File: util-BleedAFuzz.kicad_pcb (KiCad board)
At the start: 2 copper layers, 9.5 x 21.2 mm, 5 parts, among them J1 Conn_01x03_Pin, Q1 BC847, Q2 BC847

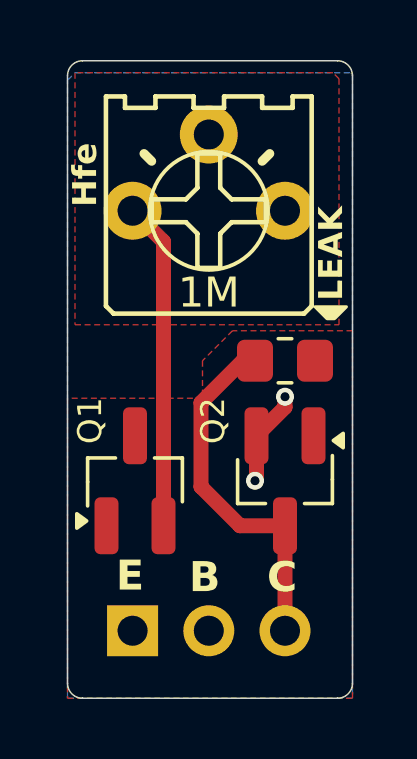
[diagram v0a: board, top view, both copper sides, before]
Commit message: Bleed-a-Fuzz: single transistor with 1M fixed + 1M trimmer base-emitter bleed
Q1 sits straight across the E-B-C header; R2 1M in series with RV1 1M
(rheostat) from base to emitter bleeds base drive so the host stage biases
as if the transistor had a lower hFE (1M..2M covers ~70..140 in a 50 uA
collector-feedback stage such as the Overcast's Q1, ~190..240 in a
fuzz-face Q1 slot). R1 2.2M collector-base (DNP) is the leakage stand-in.
Thermal-relief DRC errors on RV1 pad 1 fixed; silk renamed.

Co-Authored-By: Claude Fable 5.1 <noreply@anthropic.com>
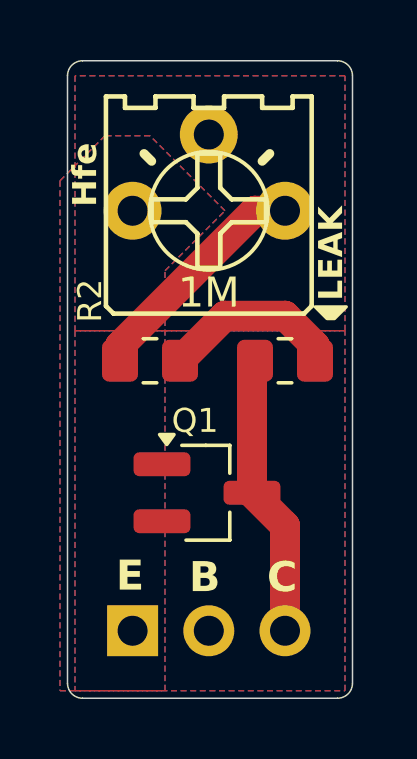
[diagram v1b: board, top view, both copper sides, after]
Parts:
- removed Q2: BC847, Package_TO_SOT_SMD:SOT-23_Handsoldering
- added R1: 2.2M, Resistor_SMD:R_0805_2012Metric_Pad1.20x1.40mm_HandSolder, F.Cu at (103.0, 79.0)
- R2: value 2.2M -> 1M
- moved R2 4.50 mm to (98.5, 79.0), turned to 180 degrees
- moved Q1 2.43 mm to (100.4, 83.4), turned to 0 degrees
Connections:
- Q1 pad 2: Net-(Q1-E) -> EMITTER
- Q1 pad 3: BASE -> COLLECTOR
- R2 pad 1: COLLECTOR -> BASE
- R2 pad 2: BASE -> Net-(R2-Pad2)
- RV1 pad 1: Net-(Q1-E) -> EMITTER
- RV1 pad 2: EMITTER -> Net-(R2-Pad2)
- RV1 pad 3: EMITTER -> Net-(R2-Pad2)
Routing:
- net Net-(Q1-E): track 10.9 -> 0.00 mm
- net Net-(R2-Pad2): track 0.00 -> 7.86 mm
- net BASE: track 0.00 -> 6.04 mm
- net EMITTER: track 3.21 -> 0.00 mm, vias 2 -> 0
- net COLLECTOR: track 12.0 -> 9.32 mm
- added copper zone on B.Cu, net BASE
- added copper zone on F.Cu, net EMITTER
- added copper zone on B.Cu, net Net-(R2-Pad2)
- added copper zone on F.Cu, net Net-(R2-Pad2)
- removed copper zone on F.Cu, net Net-(Q1-E)
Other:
- board text added: "z2a Bleed-a-Fuzz"
- board text removed: "z2a Dial-a-Fuzz"
